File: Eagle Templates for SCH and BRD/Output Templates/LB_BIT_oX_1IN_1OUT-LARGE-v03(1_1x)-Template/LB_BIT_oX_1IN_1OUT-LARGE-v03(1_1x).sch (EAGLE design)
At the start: 16 parts, among them U1 LV321SOT23-5, U2 LV321SOT23-5

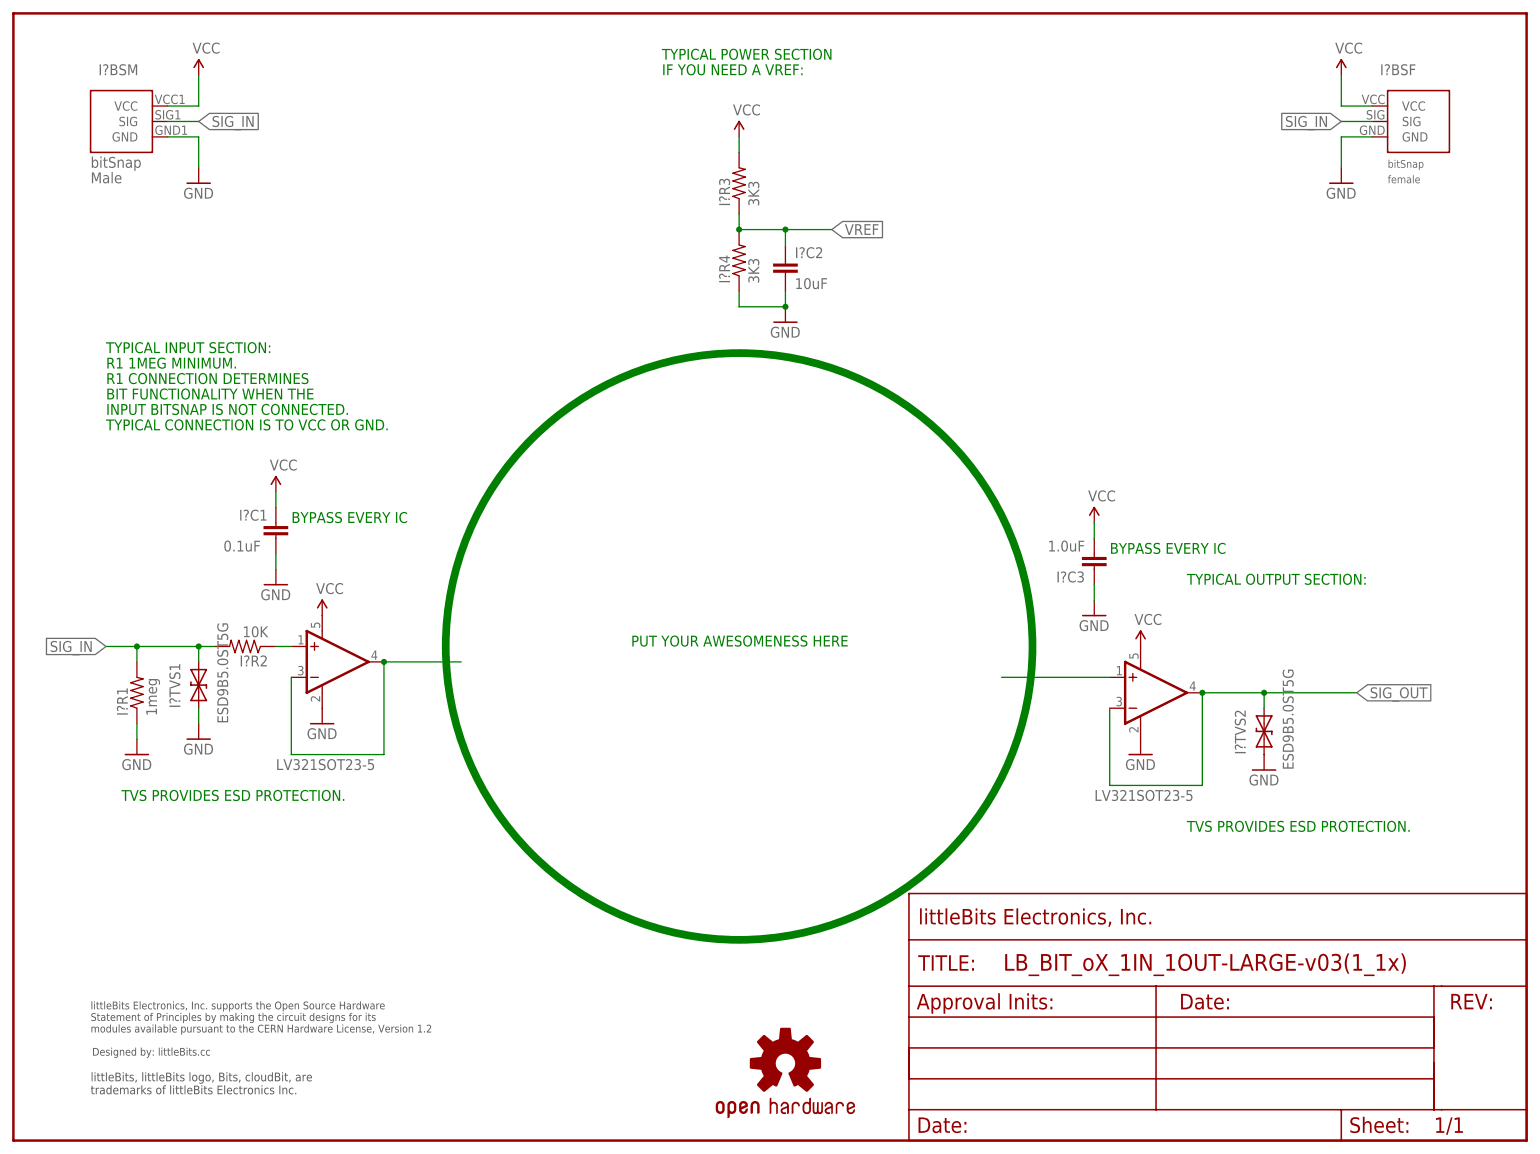
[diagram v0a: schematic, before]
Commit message: Updated templates
- Added ferrite beads
- Moved text and annotations off of Nets layer
- Minor layout changes
- Removed I/O/W prefix from reference designators
- Removed output stage components from output bits
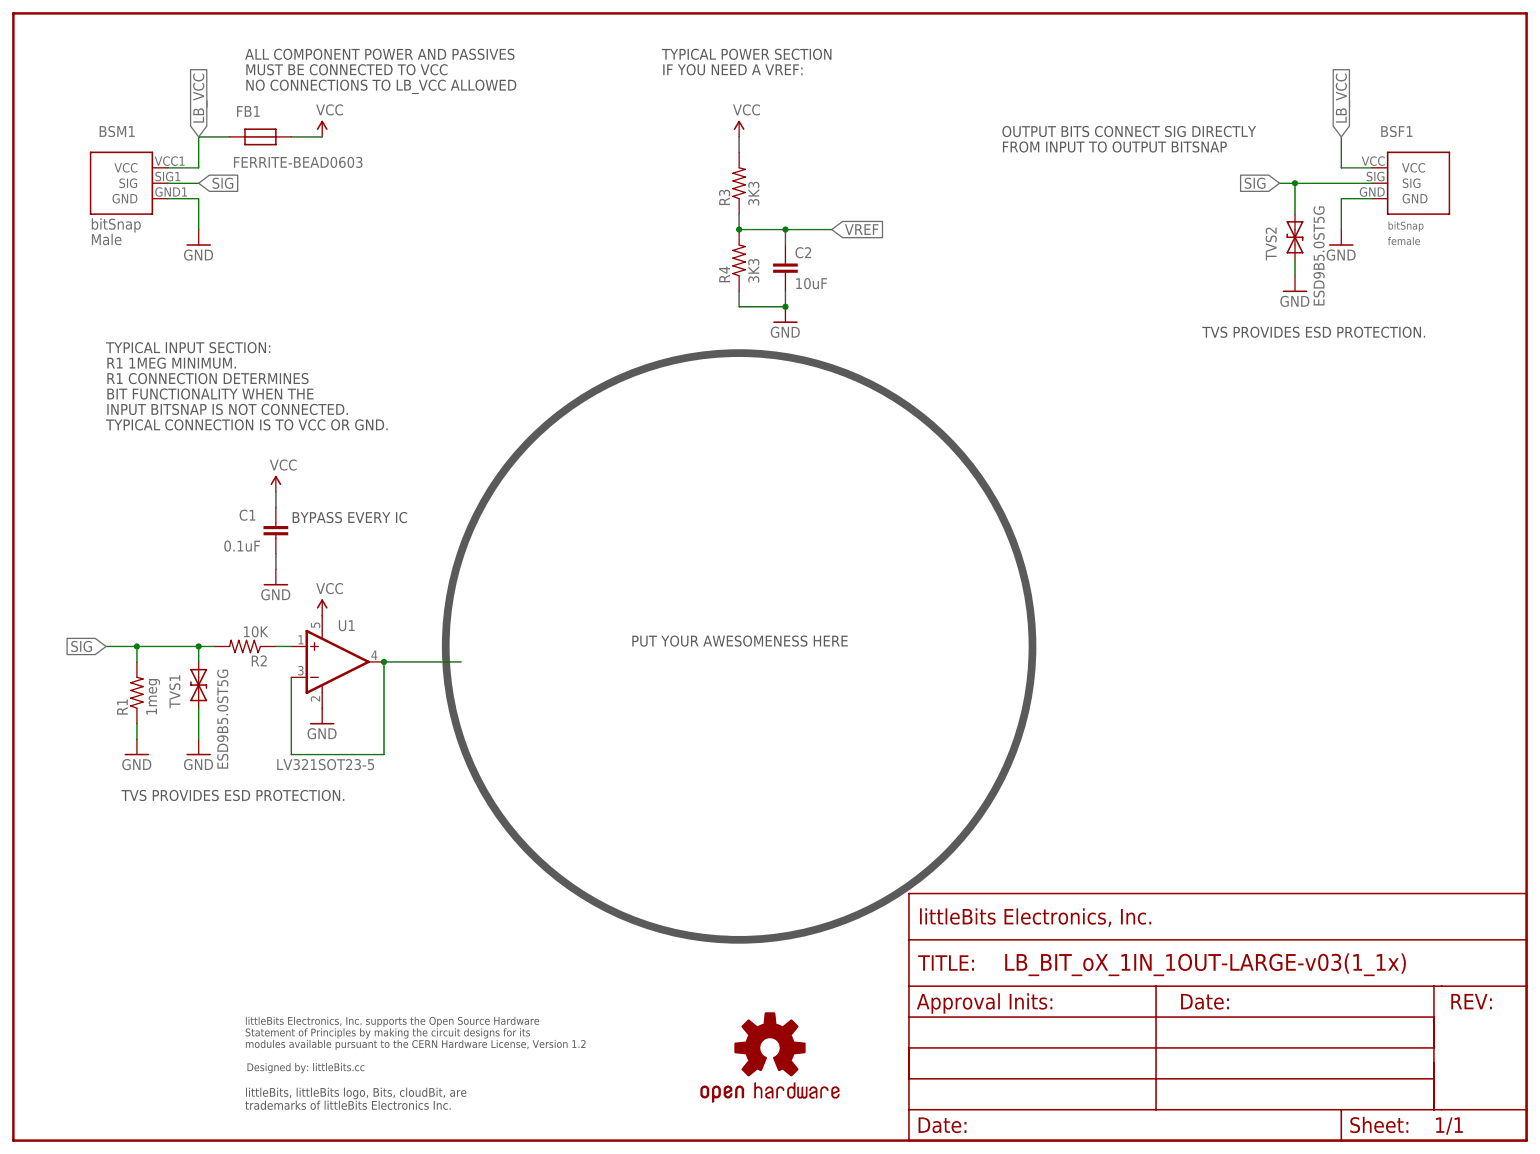
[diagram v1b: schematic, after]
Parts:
- removed I?BSF: BITSNAP_V03_FEMALE, bitSnap:BITSNAP_V03_FEMALE
- removed I?BSM: BITSNAP_V03_MALE, bitSnap:BITSNAP_V03_MALE
- removed I?C3: 1.0uF, LITTLEBITS:CAPCAP-0603
- removed I?TVS2: ESD9B5.0ST5G, LITTLEBITS:DIODE-TVSSOD-923
- removed U2: LV321SOT23-5, LITTLEBITS:LV321SOT23-5
- added BSF1: BITSNAP_V03_FEMALE, bitSnap:BITSNAP_V03_FEMALE
- added BSM1: BITSNAP_V03_MALE, bitSnap:BITSNAP_V03_MALE
- added FB1: FERRITE-BEAD0603, LITTLEBITS:FERRITE-BEAD0603
- added TVS2: ESD9B5.0ST5G, LITTLEBITS:DIODE-TVSSOD-923
- U$1: value OSHWCREDIT -> OSHW-LOGOL; device LITTLEBITS:OSHWCREDIT -> LITTLEBITS131206:OSHW-LOGOL
- U$2: value FRAME-LETTER -> OSHWCREDIT; device LITTLEBITS:FRAME-LETTER -> LITTLEBITS:OSHWCREDIT
- U$3: value OSHW-LOGOL -> FRAME-LETTER; device LITTLEBITS131206:OSHW-LOGOL -> LITTLEBITS:FRAME-LETTER
- renumbered I?C1 to C1, I?C2 to C2, I?R1 to R1, I?R2 to R2, I?R3 to R3, I?R4 to R4, I?TVS1 to TVS1
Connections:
- removed net N$3: U2.+IN
- removed net SIG_IN: I?BSF.SIG, I?BSM.SIG, R1.2, R2.2, TVS1.C
- removed net SIG_OUT: I?TVS2.C, U2.-IN, U2.OUT
- new net LB_VCC: BSF1.VCC, BSM1.VCC, FB1.P$2
- new net SIG: BSF1.SIG, BSM1.SIG, R1.2, R2.2, TVS1.C, TVS2.C
- net GND: now also BSF1.GND, BSM1.GND, TVS2.A; no longer I?BSF.GND, I?BSM.GND, I?C3.1, I?TVS2.A, U2.V-
- net VCC: now also FB1.P$1; no longer I?BSF.VCC, I?BSM.VCC, I?C3.2, U2.V+
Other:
- note added: "ALL COMPONENT POWER AND PASSIVES"
- note added: "FROM INPUT TO OUTPUT BITSNAP"
- note added: "MUST BE CONNECTED TO VCC"
- note added: "NO CONNECTIONS TO LB_VCC ALLOWED"
- note added: "OUTPUT BITS CONNECT SIG DIRECTLY"
- note removed: "TYPICAL OUTPUT SECTION:"
